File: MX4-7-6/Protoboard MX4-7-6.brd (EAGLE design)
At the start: 54.2 x 59.2 mm, 308 parts, among them J1 DCJ0202

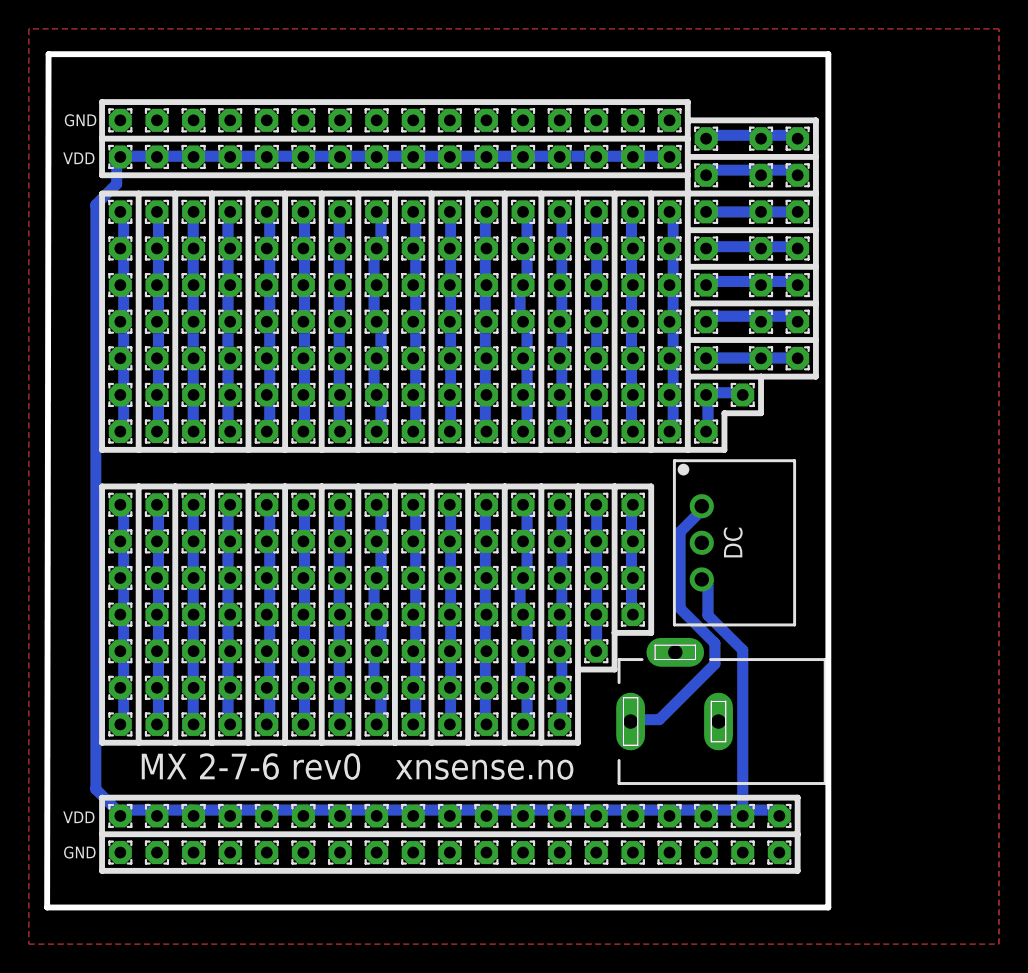
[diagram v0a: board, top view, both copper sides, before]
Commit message: Adjusted Polygon
Adjusted Polygon on all boxes. Changed length on MX-4-7-6 to fit the
box, it was 2mm to long.
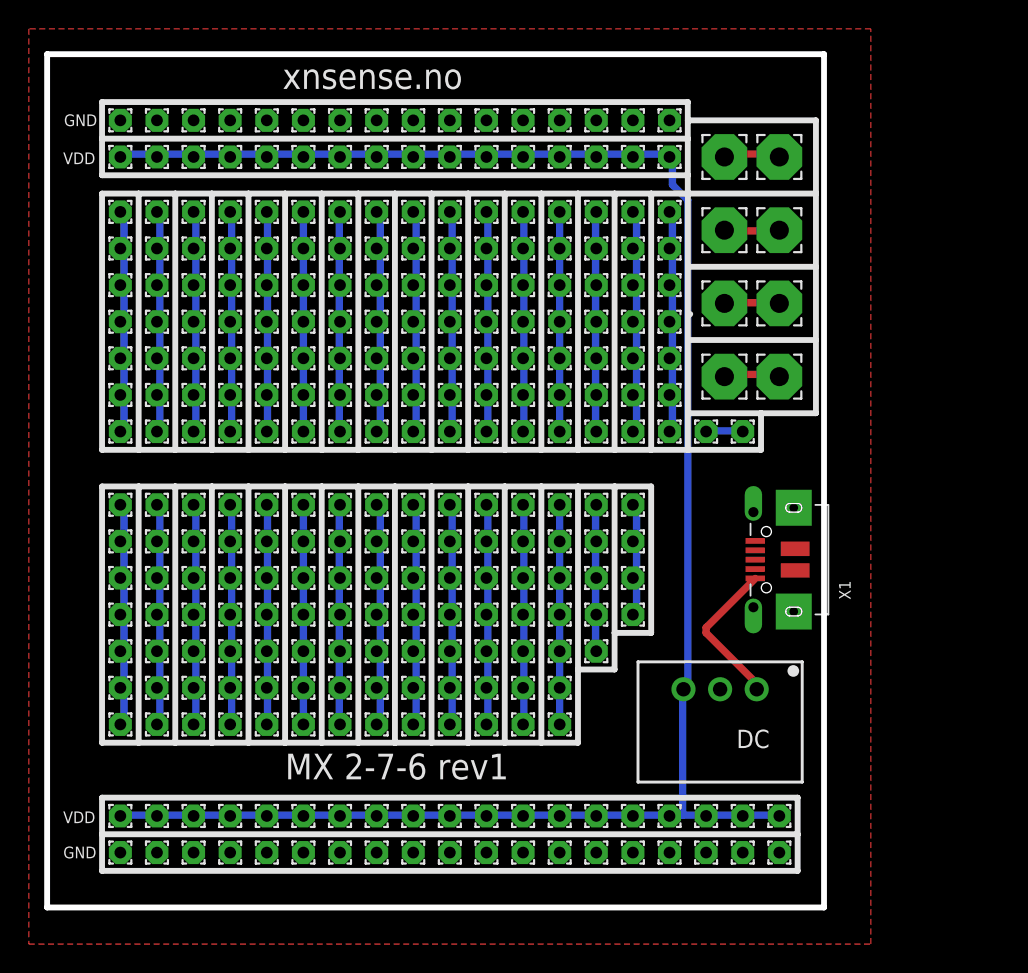
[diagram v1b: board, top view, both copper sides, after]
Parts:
- removed J1: DCJ0202, con-jack:DCJ0202
- removed PAD3, PAD396, PAD397, PAD398, PAD399, PAD400, PAD401, PAD402, PAD403, PAD404, PAD405, PAD406, PAD407, PAD408, PAD409, PAD410, PAD411, PAD412, PAD413, PAD417, PAD418, PAD419: (no value), wirepad:1,6/0,8
- added PAD34, PAD35, PAD39, PAD40, PAD42, PAD43, PAD45, PAD46: (no value), wirepad:3,17/1,3
- added X1: (no value), microbuilder:4UCONN_20329
- moved DC 10.2 mm to (46.7, 15.1), turned to 180 degrees
- moved PAD1 3.59 mm to (48.3, 33.0)
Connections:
- removed net N$42: PAD396.1, PAD397.1, PAD406.1
- removed net N$43: PAD398.1, PAD399.1, PAD407.1
- removed net N$44: PAD400.1, PAD401.1, PAD405.1
- removed net N$46: PAD408.1, PAD409.1, PAD418.1
- removed net N$47: PAD410.1, PAD411.1, PAD419.1
- removed net N$48: PAD412.1, PAD413.1, PAD417.1
- new net N$4: PAD39.1, PAD40.1
- new net N$5: PAD42.1, PAD43.1
- new net N$6: PAD45.1, PAD46.1
- net GND: now also X1.BASE@1, X1.BASE@2, X1.GND, X1.SPRT@1, X1.SPRT@2, X1.SPRT@3, X1.SPRT@4; no longer J1.2, J1.3
- net N$2: now also PAD34.1, PAD35.1; no longer PAD402.1, PAD403.1, PAD404.1
- net N$3: no longer PAD3.1
- net VCC: now also X1.VBUS; no longer J1.1
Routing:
- net VDD: track 157.3 -> 133.6 mm
- net VCC: track 20.1 -> 10.6 mm
- net N$43: track 7.19 -> 0.00 mm
- net N$48: track 7.11 -> 0.00 mm
- net N$44: track 6.80 -> 0.00 mm
- net N$47: track 6.73 -> 0.00 mm
- net N$42: track 6.36 -> 0.00 mm
- net N$46: track 6.35 -> 0.00 mm
- net N$6: track 0.00 -> 3.88 mm
- net N$5: track 0.00 -> 3.82 mm
- net N$4: track 0.00 -> 3.82 mm
- net N$3: track 5.35 -> 2.55 mm
- net N$2: track 6.49 -> 3.93 mm
- net N$15: track 17.0 -> 15.4 mm
- net N$22: track 15.6 -> 16.9 mm
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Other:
- board size 54.2 x 59.2 mm -> 53.9 x 59.2 mm
- board text added: "MX 2-7-6 rev1"
- board text removed: "MX 2-7-6 rev0"

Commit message: Update to rev2
Updated to Pin headers instead of single wire pads
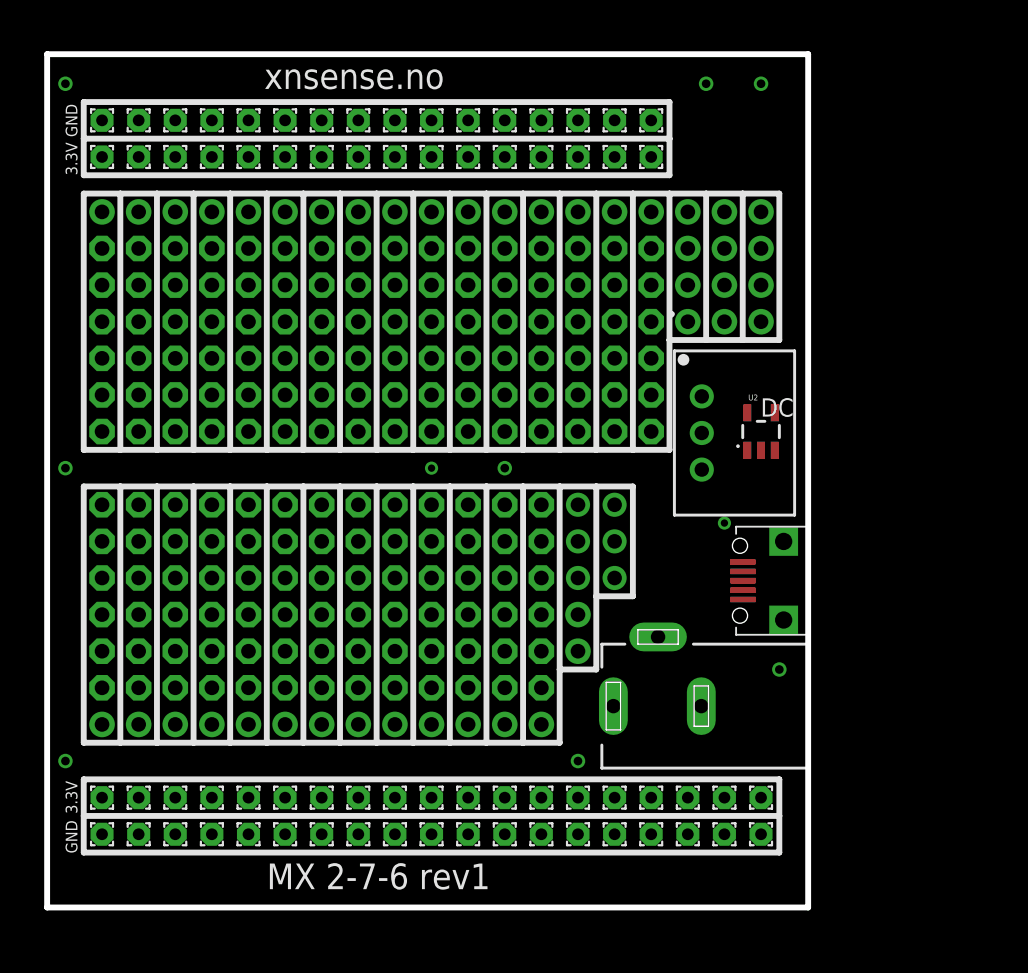
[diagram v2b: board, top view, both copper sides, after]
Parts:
- removed PAD1, PAD100, PAD101, PAD102, PAD103, PAD106, PAD107, PAD108, PAD109, PAD110, PAD111, PAD112, PAD115, PAD116, PAD117, PAD118, PAD119, PAD120, PAD121, PAD124, PAD125, PAD126, PAD127, PAD128, PAD129, PAD130, PAD133, PAD134, PAD135, PAD136, PAD137, PAD138, PAD139, PAD142, PAD143, PAD144, PAD145, PAD146, PAD147, PAD148, PAD151, PAD152, PAD153, PAD154, PAD155, PAD156, PAD157, PAD160, PAD161, PAD162, PAD163, PAD164, PAD165, PAD166, PAD169, PAD170, PAD171, PAD172, PAD173, PAD174, PAD175, PAD178, PAD179, PAD180, PAD181, PAD182, PAD183, PAD184, PAD187, PAD188, PAD189, PAD190, PAD191, PAD192, PAD193, PAD196, PAD197, PAD198, PAD199, PAD2, PAD200, PAD201, PAD202, PAD205, PAD206, PAD207, PAD208, PAD209, PAD210, PAD211, PAD214, PAD215, PAD216, PAD217, PAD218, PAD219, PAD220, PAD260, PAD261, PAD262, PAD263, PAD264, PAD265, PAD266, PAD269, PAD270, PAD271, PAD272, PAD273, PAD274, PAD275, PAD278, PAD279, PAD280, PAD281, PAD282, PAD283, PAD284, PAD287, PAD288, PAD289, PAD290, PAD291, PAD292, PAD293, PAD296, PAD297, PAD298, PAD299, PAD300, PAD301, PAD302, PAD305, PAD306, PAD307, PAD308, PAD309, PAD310, PAD311, PAD314, PAD315, PAD316, PAD317, PAD318, PAD319, PAD320, PAD332, PAD333, PAD334, PAD335, PAD336, PAD337, PAD338, PAD341, PAD342, PAD343, PAD344, PAD345, PAD346, PAD347, PAD350, PAD351, PAD352, PAD353, PAD354, PAD355, PAD356, PAD359, PAD360, PAD361, PAD362, PAD363, PAD364, PAD365, PAD368, PAD369, PAD370, PAD371, PAD372, PAD373, PAD374, PAD377, PAD378, PAD379, PAD380, PAD381, PAD382, PAD383, PAD385, PAD386, PAD387, PAD388, PAD389, PAD391, PAD392, PAD393, PAD394, PAD79, PAD80, PAD81, PAD82, PAD83, PAD84, PAD85, PAD88, PAD89, PAD90, PAD91, PAD92, PAD93, PAD94, PAD97, PAD98, PAD99: (no value), wirepad:1,6/0,8
- removed PAD34, PAD35, PAD39, PAD40, PAD42, PAD43, PAD45, PAD46: (no value), wirepad:3,17/1,3
- removed X1: (no value), microbuilder:4UCONN_20329
- added CN1, CN2, CN3: 1X4-CLEANBIG, adafruit:1X04-CLEANBIG
- added J1: DCJ0202, con-jack:DCJ0202
- added JP1: USB-RECEPTABLE, daspilker:FCI-10103594-0001LF
- added JP10, JP11, JP12, JP13, JP14, JP15, JP16, JP17, JP18, JP19, JP2, JP20, JP21, JP22, JP23, JP24, JP25, JP26, JP27, JP28, JP29, JP3, JP30, JP4, JP5, JP6, JP7, JP8, JP9: (no value), adafruit:1X06-CLEANBIG
- added JP31, JP32: (no value), adafruit:1X03-CLEANBIG
- added JP33, JP34, JP35, JP36, JP37, JP38, JP39, JP40, JP41, JP42, JP43, JP44, JP45, JP46, JP47, JP48, JP49, JP50, JP51, JP52, JP53, JP54, JP55, JP56, JP57, JP58, JP59, JP60, JP61, JP62, JP63: (no value), adafruit:1X01-CLEANBIG
- added U2: (no value), SparkFun-PowerIC:SOT23-5
- moved DC 17.8 mm to (45.4, 32.9), turned to 270 degrees
- moved PAD443 1.80 mm to (39.4, 7.62)
- moved PAD445 1.80 mm to (41.9, 7.62)
- moved PAD446 1.80 mm to (36.8, 7.62)
- moved PAD449 1.80 mm to (34.3, 7.62)
- moved PAD452 1.80 mm to (31.8, 7.62)
- moved PAD425 1.80 mm to (41.9, 5.08)
- moved PAD430 1.80 mm to (36.8, 5.08)
- moved PAD433 1.80 mm to (39.4, 5.08)
- moved PAD436 1.80 mm to (34.3, 5.08)
- moved PAD439 1.80 mm to (31.8, 5.08)
- moved PAD447 1.80 mm to (6.35, 7.62)
- moved PAD424 1.80 mm to (6.35, 5.08)
- moved PAD444 1.80 mm to (3.81, 7.62)
- moved PAD421 1.80 mm to (3.81, 5.08)
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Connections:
- removed net N$40: PAD377.1, PAD378.1, PAD379.1, PAD380.1, PAD381.1, PAD382.1, PAD383.1
- removed net N$41: PAD385.1, PAD386.1, PAD387.1, PAD388.1, PAD389.1
- net GND: now also J1.2, J1.3, JP1.5, U2.2; no longer X1.BASE@1, X1.BASE@2, X1.GND, X1.SPRT@1, X1.SPRT@2, X1.SPRT@3, X1.SPRT@4
- net N$1: now also JP2.1, JP2.2, JP2.3, JP2.4, JP2.5, JP2.6, JP48.1; no longer PAD391.1, PAD392.1, PAD393.1, PAD394.1
- net N$10: now also JP54.1, JP9.1, JP9.2, JP9.3, JP9.4, JP9.5, JP9.6; no longer PAD106.1, PAD107.1, PAD108.1, PAD109.1, PAD110.1, PAD111.1, PAD112.1
- net N$11: now also JP10.1, JP10.2, JP10.3, JP10.4, JP10.5, JP10.6, JP55.1; no longer PAD115.1, PAD116.1, PAD117.1, PAD118.1, PAD119.1, PAD120.1, PAD121.1
- net N$12: now also JP11.1, JP11.2, JP11.3, JP11.4, JP11.5, JP11.6, JP56.1; no longer PAD124.1, PAD125.1, PAD126.1, PAD127.1, PAD128.1, PAD129.1, PAD130.1
- net N$13: now also JP12.1, JP12.2, JP12.3, JP12.4, JP12.5, JP12.6, JP57.1; no longer PAD133.1, PAD134.1, PAD135.1, PAD136.1, PAD137.1, PAD138.1, PAD139.1
- net N$14: now also JP13.1, JP13.2, JP13.3, JP13.4, JP13.5, JP13.6, JP58.1; no longer PAD142.1, PAD143.1, PAD144.1, PAD145.1, PAD146.1, PAD147.1, PAD148.1
- net N$15: now also JP14.1, JP14.2, JP14.3, JP14.4, JP14.5, JP14.6, JP59.1; no longer PAD151.1, PAD152.1, PAD153.1, PAD154.1, PAD155.1, PAD156.1, PAD157.1
- net N$16: now also JP15.1, JP15.2, JP15.3, JP15.4, JP15.5, JP15.6, JP60.1; no longer PAD160.1, PAD161.1, PAD162.1, PAD163.1, PAD164.1, PAD165.1, PAD166.1
- net N$17: now also JP16.1, JP16.2, JP16.3, JP16.4, JP16.5, JP16.6, JP61.1; no longer PAD169.1, PAD170.1, PAD171.1, PAD172.1, PAD173.1, PAD174.1, PAD175.1
- net N$18: now also JP4.1, JP4.2, JP4.3, JP4.4, JP4.5, JP4.6, JP62.1; no longer PAD178.1, PAD179.1, PAD180.1, PAD181.1, PAD182.1, PAD183.1, PAD184.1
- net N$19: now also JP17.1, JP17.2, JP17.3, JP17.4, JP17.5, JP17.6, JP63.1; no longer PAD187.1, PAD188.1, PAD189.1, PAD190.1, PAD191.1, PAD192.1, PAD193.1
- net N$2: now also CN1.1, CN1.2, CN1.3, CN1.4; no longer PAD34.1, PAD35.1
- net N$20: now also JP18.1, JP18.2, JP18.3, JP18.4, JP18.5, JP18.6, JP34.1; no longer PAD196.1, PAD197.1, PAD198.1, PAD199.1, PAD200.1, PAD201.1, PAD202.1
- net N$21: now also JP19.1, JP19.2, JP19.3, JP19.4, JP19.5, JP19.6, JP35.1; no longer PAD205.1, PAD206.1, PAD207.1, PAD208.1, PAD209.1, PAD210.1, PAD211.1
- net N$22: now also JP20.1, JP20.2, JP20.3, JP20.4, JP20.5, JP20.6, JP36.1; no longer PAD214.1, PAD215.1, PAD216.1, PAD217.1, PAD218.1, PAD219.1, PAD220.1
- net N$27: now also JP21.1, JP21.2, JP21.3, JP21.4, JP21.5, JP21.6, JP37.1; no longer PAD260.1, PAD261.1, PAD262.1, PAD263.1, PAD264.1, PAD265.1, PAD266.1
- net N$28: now also JP22.1, JP22.2, JP22.3, JP22.4, JP22.5, JP22.6, JP38.1; no longer PAD269.1, PAD270.1, PAD271.1, PAD272.1, PAD273.1, PAD274.1, PAD275.1
- net N$29: now also JP23.1, JP23.2, JP23.3, JP23.4, JP23.5, JP23.6, JP39.1; no longer PAD278.1, PAD279.1, PAD280.1, PAD281.1, PAD282.1, PAD283.1, PAD284.1
- net N$3: now also CN2.1, CN2.2, CN2.3, CN2.4; no longer PAD1.1, PAD2.1
- net N$30: now also JP24.1, JP24.2, JP24.3, JP24.4, JP24.5, JP24.6, JP40.1; no longer PAD287.1, PAD288.1, PAD289.1, PAD290.1, PAD291.1, PAD292.1, PAD293.1
- net N$31: now also JP25.1, JP25.2, JP25.3, JP25.4, JP25.5, JP25.6, JP41.1; no longer PAD296.1, PAD297.1, PAD298.1, PAD299.1, PAD300.1, PAD301.1, PAD302.1
- net N$32: now also JP26.1, JP26.2, JP26.3, JP26.4, JP26.5, JP26.6, JP42.1; no longer PAD305.1, PAD306.1, PAD307.1, PAD308.1, PAD309.1, PAD310.1, PAD311.1
- net N$33: now also JP27.1, JP27.2, JP27.3, JP27.4, JP27.5, JP27.6, JP43.1; no longer PAD314.1, PAD315.1, PAD316.1, PAD317.1, PAD318.1, PAD319.1, PAD320.1
- net N$35: now also JP28.1, JP28.2, JP28.3, JP28.4, JP28.5, JP28.6, JP44.1; no longer PAD332.1, PAD333.1, PAD334.1, PAD335.1, PAD336.1, PAD337.1, PAD338.1
- net N$36: now also JP29.1, JP29.2, JP29.3, JP29.4, JP29.5, JP29.6, JP45.1; no longer PAD341.1, PAD342.1, PAD343.1, PAD344.1, PAD345.1, PAD346.1, PAD347.1
- net N$37: now also JP30.1, JP30.2, JP30.3, JP30.4, JP30.5, JP30.6, JP46.1; no longer PAD350.1, PAD351.1, PAD352.1, PAD353.1, PAD354.1, PAD355.1, PAD356.1
- net N$38: now also JP31.1, JP31.2, JP31.3, JP33.1, JP47.1; no longer PAD359.1, PAD360.1, PAD361.1, PAD362.1, PAD363.1, PAD364.1, PAD365.1
- net N$39: now also JP32.1, JP32.2, JP32.3; no longer PAD368.1, PAD369.1, PAD370.1, PAD371.1, PAD372.1, PAD373.1, PAD374.1
- net N$4: now also CN3.1, CN3.2, CN3.3, CN3.4; no longer PAD39.1, PAD40.1
- net N$5: now also JP3.1, JP3.2, JP3.3, JP3.4, JP3.5, JP3.6, JP49.1; no longer PAD42.1, PAD43.1
- net N$6: now also JP5.1, JP5.2, JP5.3, JP5.4, JP5.5, JP5.6, JP50.1; no longer PAD45.1, PAD46.1
- net N$7: now also JP51.1, JP6.1, JP6.2, JP6.3, JP6.4, JP6.5, JP6.6; no longer PAD79.1, PAD80.1, PAD81.1, PAD82.1, PAD83.1, PAD84.1, PAD85.1
- net N$8: now also JP52.1, JP7.1, JP7.2, JP7.3, JP7.4, JP7.5, JP7.6; no longer PAD88.1, PAD89.1, PAD90.1, PAD91.1, PAD92.1, PAD93.1, PAD94.1
- net N$9: now also JP53.1, JP8.1, JP8.2, JP8.3, JP8.4, JP8.5, JP8.6; no longer PAD100.1, PAD101.1, PAD102.1, PAD103.1, PAD97.1, PAD98.1, PAD99.1
- net VCC: now also J1.1, JP1.1, U2.1, U2.3; no longer X1.VBUS
- net VDD: now also U2.5
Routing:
- net VDD: track 133.6 -> 0.00 mm
- net N$40: track 16.9 -> 0.00 mm, vias 0 -> 1
- net N$27: track 16.9 -> 0.00 mm
- net N$17: track 16.9 -> 0.00 mm
- net N$9: track 16.9 -> 0.00 mm
- net N$22: track 16.9 -> 0.00 mm
- net N$35: track 16.5 -> 0.00 mm
- net N$28: track 16.5 -> 0.00 mm
- net N$21: track 16.5 -> 0.00 mm
- net N$12: track 16.5 -> 0.00 mm
- net N$10: track 16.5 -> 0.00 mm
- net N$36: track 16.1 -> 0.00 mm
- net N$29: track 16.1 -> 0.00 mm
- net N$7: track 16.0 -> 0.00 mm
- net N$13: track 16.0 -> 0.00 mm
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- added copper zone on layer 16, net N$45
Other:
- board size 53.9 x 59.2 mm -> 52.8 x 59.2 mm
- board text added: "3.3V"
- board text removed: "VDD"

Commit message: Change usb connector
Change to correct usb connecter and moved esp8266 bit more onto the
board.
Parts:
- removed JP1: USB-RECEPTABLE, daspilker:FCI-10103594-0001LF
- added X1: (no value), microbuilder:4UCONN_20329
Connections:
- net GND: now also X1.BASE@1, X1.BASE@2, X1.GND, X1.SPRT@1, X1.SPRT@2, X1.SPRT@3, X1.SPRT@4; no longer JP1.5
- net VCC: now also X1.VBUS; no longer JP1.1

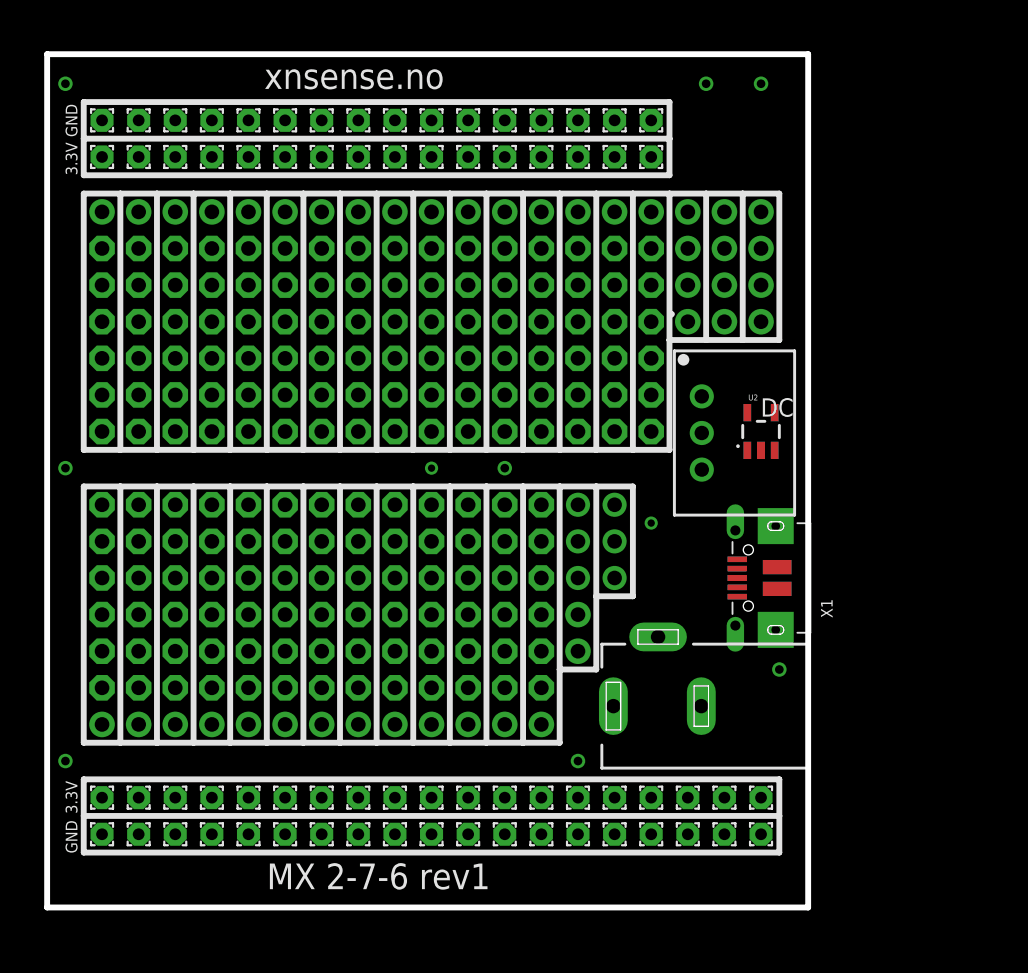
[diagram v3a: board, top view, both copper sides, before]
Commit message: Routing and Gerber files
Routed and produced gerber files
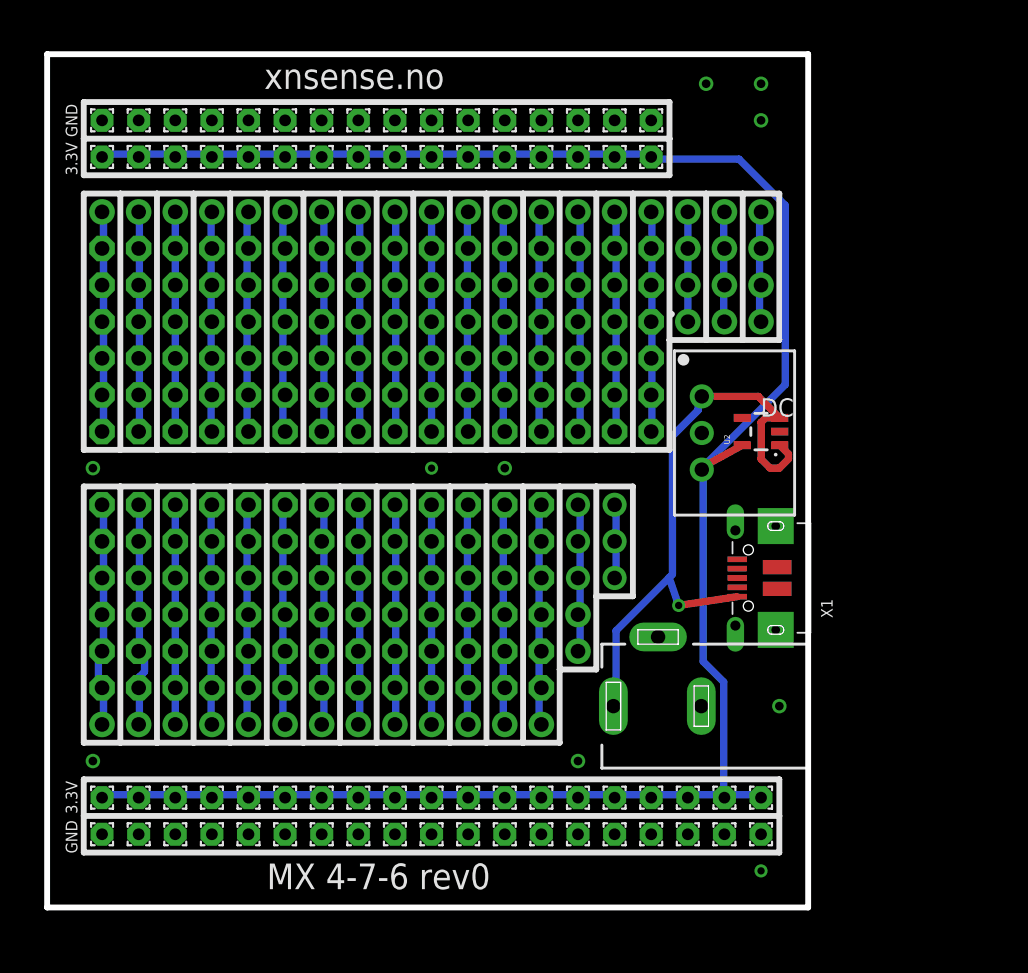
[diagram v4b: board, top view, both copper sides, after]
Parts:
- turned U2 to 90 degrees
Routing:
- net VDD: track 0.00 -> 148.3 mm, vias 0 -> 1
- net VCC: track 0.00 -> 43.8 mm, vias 0 -> 1
- net N$20: track 0.00 -> 16.1 mm
- net N$37: track 0.00 -> 16.1 mm
- net N$30: track 0.00 -> 16.1 mm
- net N$29: track 0.00 -> 16.1 mm
- net N$9: track 0.00 -> 16.0 mm
- net N$8: track 0.00 -> 16.0 mm
- net N$16: track 0.00 -> 16.0 mm
- net N$15: track 0.00 -> 16.0 mm
- net N$21: track 0.00 -> 15.7 mm
- net N$36: track 0.00 -> 15.7 mm
- net N$31: track 0.00 -> 15.7 mm
- net N$28: track 0.00 -> 15.7 mm
- net N$17: track 0.00 -> 15.7 mm
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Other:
- board text added: "MX 4-7-6 rev0"
- board text removed: "MX 2-7-6 rev1"
